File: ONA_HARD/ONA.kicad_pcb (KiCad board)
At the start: 4 copper layers, 78.3 x 45.3 mm, 53 parts

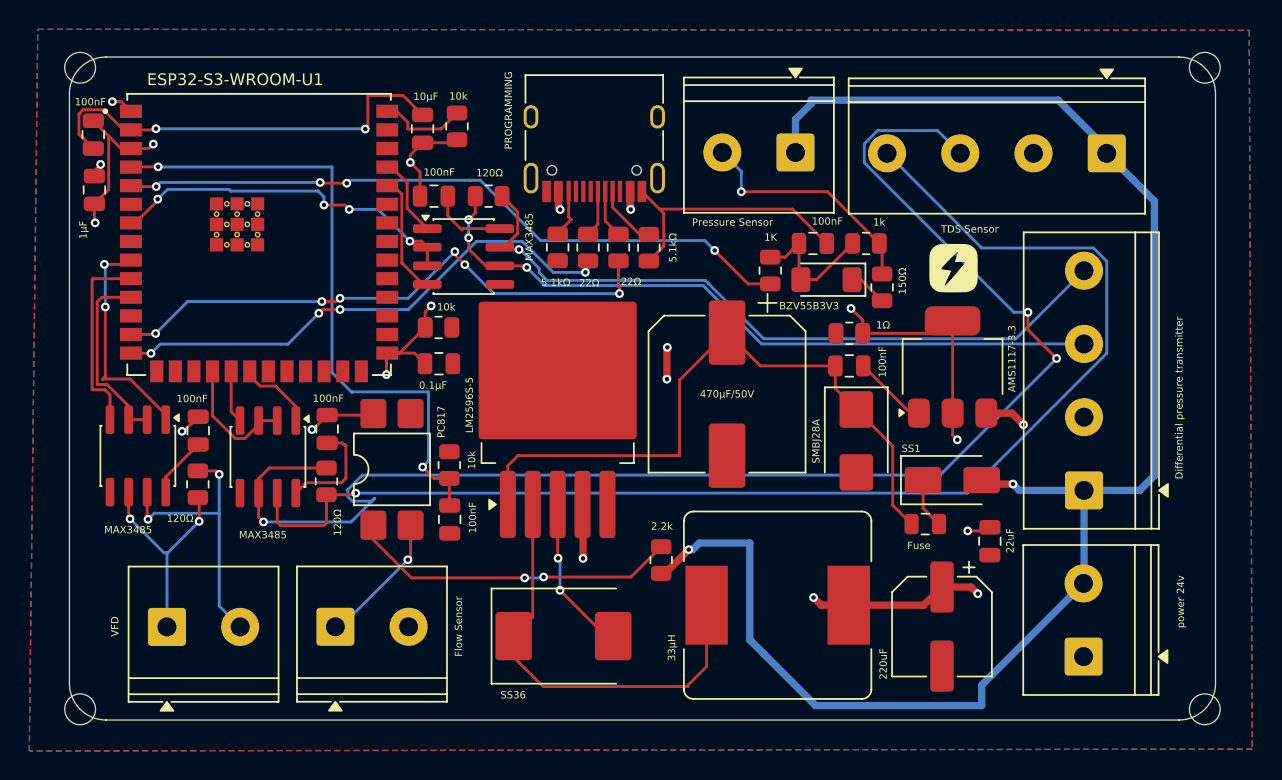
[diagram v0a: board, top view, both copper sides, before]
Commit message: chore: remove .history folders and add to gitignore
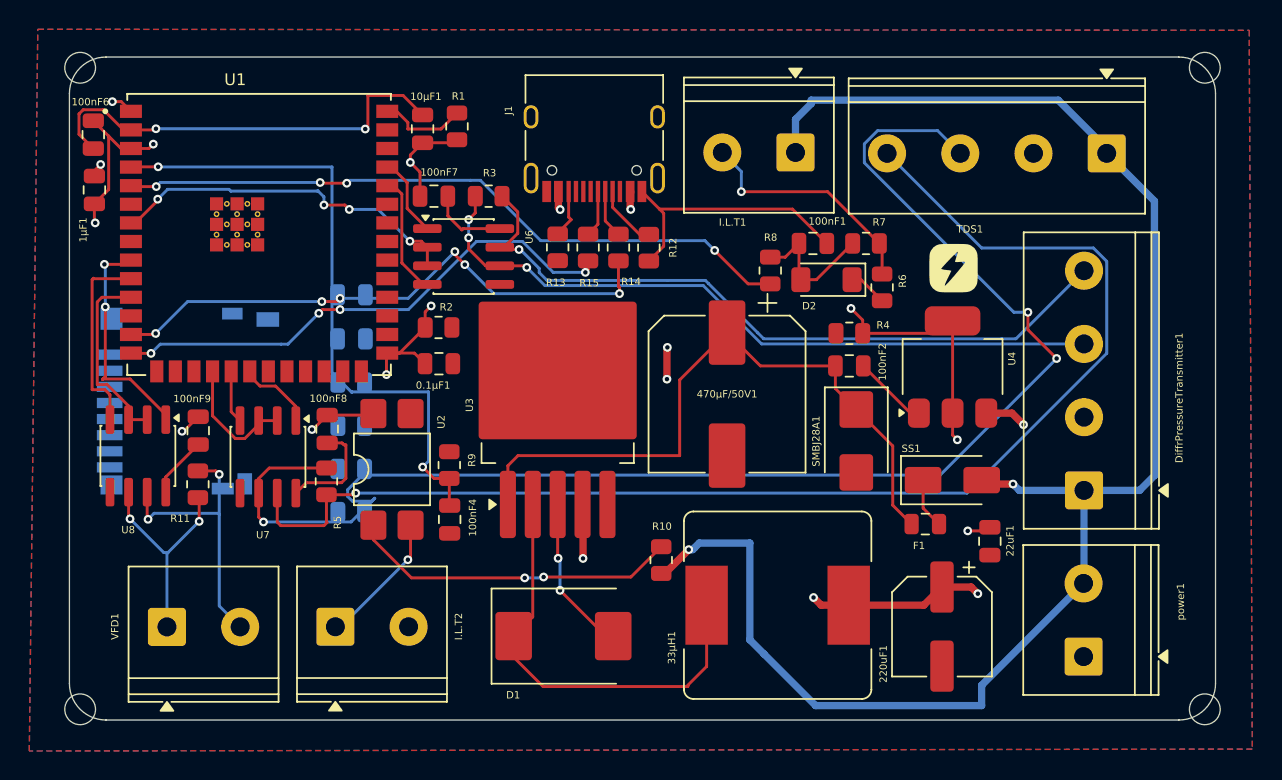
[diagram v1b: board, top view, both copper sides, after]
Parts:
- added 100nF10: C, Capacitor_SMD:C_0805_2012Metric, B.Cu at (124.5, 105.0)
- added 10μF2: C, Capacitor_SMD:C_0805_2012Metric, B.Cu at (124.5, 102.0)
- added J3: Micro_SD_Card, Connector_Card:microSD_HC_Hirose_DM3D-SF, B.Cu at (113.4, 109.3)
- added R22: 10kΩ, Resistor_SMD:R_0805_2012Metric, B.Cu at (124.5, 116.8)
- added R23: 10kΩ, Resistor_SMD:R_0805_2012Metric, B.Cu at (124.5, 113.9)
- added R29: 10kΩ, Resistor_SMD:R_0805_2012Metric, B.Cu at (124.5, 110.9)
- added R30: 10kΩ, Resistor_SMD:R_0805_2012Metric, B.Cu at (124.5, 108.0)
- DiffrPressureTransmitter1: renamed from Differential pressure transmitter
- I.L.T1: renamed from Pressure Sensor
- I.L.T2: renamed from Flow Sensor
- R1: renamed from 10k; value R -> 10k1
- TDS1: renamed from TDS Sensor
- power1: renamed from power 24v
- renumbered 0.1µF to 0.1µF1, 100nF to 100nF1, 100nF to 100nF2, 100nF to 100nF4, 100nF to 100nF6, 100nF to 100nF7, 100nF to 100nF8, 100nF to 100nF9, 10μF to 10μF1, 1μF to 1μF1, 220uF to 220uF1, 22uF to 22uF1, 33µH to 33µH1, 470µF/50V to 470µF/50V1, SS36 to D1, BZV55B3V3 to D2, Fuse to F1, PROGRAMMING to J1, 2.2k to R10, 120Ω to R11, 5.1kΩ to R12, 5.1kΩ to R13, 22Ω to R14, 22Ω to R15, 10k to R2, 120Ω to R3, 1Ω to R4, 120Ω to R5, 150Ω to R6, 1k to R7, 1K to R8, 10k to R9, SMBJ28A to SMBJ28A1, ESP32-S3-WROOM-U1 to U1, PC817 to U2, LM2596S-5 to U3, AMS1117-3.3 to U4, MAX3485 to U6, MAX3485 to U7, MAX3485 to U8, VFD to VFD1
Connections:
- U1 pad 16: unconnected-(U1-IO46-Pad16) -> /CMD
- U1 pad 31: unconnected-(U1-IO38-Pad31) -> /CLK
- U1 pad 32: unconnected-(U1-IO39-Pad32) -> /3.3v
- U1 pad 33: unconnected-(U1-IO40-Pad33) -> /3.3v
- U1 pad 34: unconnected-(U1-IO41-Pad34) -> /3.3v
- U1 pad 35: unconnected-(U1-IO42-Pad35) -> /3.3v
- U1 pad 41_10: GND -> (no net)
- U1 pad 41_11: GND -> (no net)
- U1 pad 41_12: GND -> (no net)
- U1 pad 41_13: GND -> (no net)
- U1 pad 41_14: GND -> (no net)
- U1 pad 41_15: GND -> (no net)
- U1 pad 41_16: GND -> (no net)
- U1 pad 41_17: GND -> (no net)
- U1 pad 41_18: GND -> (no net)
- U1 pad 41_19: GND -> (no net)
- U1 pad 41_20: GND -> (no net)
- U1 pad 41_21: GND -> (no net)
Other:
- board text added: "I.L.T"
- board text removed: "I.L.T_pin"
